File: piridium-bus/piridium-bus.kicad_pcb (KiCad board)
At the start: 2 copper layers, 52 parts, among them J1 EPS, J2 MODEM UART, J3 ANT, J4 PAYLOAD, Q1 2N7002, Q2 DMP3015LSSQ, U1 LM1117-3.3, U2 TPS54394RSAR, U3 MAX6369, U4 74LS126, U5 DS3232M

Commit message: some work on routing
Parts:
- removed H1, H2, H3, H4: M3, MountingHole:MountingHole_3.2mm_M3_DIN965_Pad
- added MH1: M3, MountingHole:MountingHole_3.2mm_M3_DIN965_Pad, F.Cu at (110.5, 55.9)
- added MH2: M3, MountingHole:MountingHole_3.2mm_M3_DIN965_Pad, F.Cu at (184.2, 55.9)
- added MH3: M3, MountingHole:MountingHole_3.2mm_M3_DIN965_Pad, F.Cu at (186.7, 141.6)
- added MH4: M3, MountingHole:MountingHole_3.2mm_M3_DIN965_Pad, F.Cu at (106.7, 141.6)
- BT1: moved to B.Cu
- C6, C7: footprint Capacitor_SMD:C_0805_2012Metric -> Capacitor_SMD:C_0603_1608Metric
- moved U2 176.1 mm to (253.5, 92.5)
- moved L2 161.9 mm to (253.0, 81.3), turned to 90 degrees
- moved C1 156.5 mm to (285.6, 103.6)
- moved C6 154.7 mm to (249.4, 94.5), turned to -90 degrees
- moved C13 150.7 mm to (316.0, 78.4)
- moved C8 148.7 mm to (301.4, 91.2)
- moved R8 147.3 mm to (311.4, 84.6)
- moved R7 143.8 mm to (301.4, 94.2)
- moved U1 140.6 mm to (287.0, 134.1)
- moved C12 137.7 mm to (252.5, 131.1)
- moved C14 137.6 mm to (276.3, 112.3)
- moved C4 137.1 mm to (251.5, 97.5)
- moved L1 136.2 mm to (253.0, 103.6), turned to 90 degrees
- moved JP1 134.1 mm to (268.7, 132.3)
- moved R3 131.7 mm to (331.7, 65.4)
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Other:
- board outline added: 90.2 x 95.9 mm

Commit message: routing work on bus
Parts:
- added R12: 10K, Resistor_SMD:R_1206_3216Metric, F.Cu at (111.3, 75.2)
- C1, C10, C11, C2, C3, C4, C5, C6, C7, C8, C9, JP1, L1, L2, R1, R2, R5, R6, TP1, TP2, TP3, TP4, U1, U2, U3: moved to B.Cu
- R10, R7, R8: footprint Resistor_SMD:R_0805_2012Metric -> Resistor_SMD:R_1206_3216Metric
- R11: value 10K -> 33K; footprint Resistor_SMD:R_0805_2012Metric -> Resistor_SMD:R_1206_3216Metric
- R3, R4: footprint Resistor_SMD:R_0805_2012Metric -> Resistor_SMD:R_1206_3216Metric; moved to B.Cu
- R9: value 10K -> 22K; footprint Resistor_SMD:R_0805_2012Metric -> Resistor_SMD:R_1206_3216Metric
- moved R3 205.9 mm to (131.0, 111.4), turned to 180 degrees
- moved D1 188.1 mm to (113.8, 75.2), turned to 90 degrees
- moved R6 183.1 mm to (124.4, 115.8)
- moved C8 178.5 mm to (124.4, 113.8)
- moved R9 169.1 mm to (138.2, 75.2)
- moved R8 157.6 mm to (155.4, 62.0), turned to -90 degrees
- moved R1 157.0 mm to (123.8, 107.7), turned to -90 degrees
- moved TP3 152.9 mm to (115.3, 132.6), turned to 90 degrees
- moved R5 152.4 mm to (123.8, 118.9), turned to 90 degrees
- moved U1 151.8 mm to (137.1, 110.3), turned to 90 degrees
- moved C10 149.4 mm to (119.3, 134.6)
- moved C1 149.0 mm to (137.1, 115.9)
- moved R7 146.5 mm to (159.0, 59.4)
- moved C11 146.5 mm to (119.3, 131.1)
- moved TP4 143.6 mm to (125.5, 132.6), turned to -90 degrees
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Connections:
- R11 pad 1: /SUP_OUT -> GND
- R11 pad 2: Net-(D1-Pad2) -> S_MODEM_ON_OFF
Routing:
- net GND: track 0.01 -> 46.1 mm, vias 0 -> 14
- net +5VP: track 0.00 -> 35.9 mm, vias 0 -> 2
- net Net-(BT1-Pad1): track 0.00 -> 35.3 mm
- net +5V: track 0.00 -> 32.5 mm, vias 0 -> 2
- net +BATT: track 0.00 -> 24.5 mm
- net Net-(C5-Pad1): track 0.00 -> 23.0 mm
- net Net-(C7-Pad2): track 0.00 -> 10.7 mm, vias 0 -> 4
- net Net-(C6-Pad2): track 0.00 -> 10.7 mm, vias 0 -> 4
- net /EN: track 0.00 -> 8.17 mm
- net Net-(R5-Pad2): track 0.00 -> 5.16 mm
- net Net-(R1-Pad2): track 0.00 -> 5.16 mm
- net Net-(JP1-Pad1): track 0.00 -> 3.76 mm
- net +3.3V: track 0.00 -> 2.90 mm
- net S_HANDSHAKE: track 0.00 -> 2.83 mm
- net /PAYLOAD_PWR: track 0.00 -> 2.54 mm
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- added copper zone on B.Cu, net GND
- added copper zone on B.Cu, net Net-(C6-Pad2)
- added copper zone on B.Cu, net Net-(C7-Pad2)
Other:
- outline, holes or cut-outs redrawn

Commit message: update routing
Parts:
- J1: footprint Connector_Molex:Molex_Nano-Fit_105313-xx04_1x04_P2.50mm_Horizontal -> Connector_PinHeader_2.54mm:PinHeader_1x04_P2.54mm_Horizontal; moved to B.Cu
- J4: footprint Connector_Molex:Molex_Nano-Fit_105314-xx10_2x05_P2.50mm_Horizontal -> Connector_PinHeader_2.54mm:PinHeader_2x05_P2.54mm_Vertical
- JP1: moved to F.Cu
- R11, R9: moved to B.Cu
- moved J2 95.6 mm to (165.9, 141.2), turned to -90 degrees
- moved J3 85.1 mm to (144.0, 140.0), turned to 180 degrees
- moved A2 71.5 mm to (166.4, 62.5), turned to 0 degrees
- moved C12 49.8 mm to (158.0, 103.9), turned to -90 degrees
- moved R12 45.3 mm to (150.4, 98.0)
- moved D1 45.3 mm to (152.9, 98.0)
- moved U4 43.1 mm to (153.1, 107.1), turned to 0 degrees
- moved A3 42.2 mm to (148.0, 88.8), turned to -90 degrees
- moved R11 34.2 mm to (135.1, 108.5), turned to -90 degrees
- moved R9 33.3 mm to (137.7, 108.5), turned to -90 degrees
- moved J4 30.3 mm to (135.9, 65.8)
- moved R7 24.0 mm to (147.6, 80.6), turned to -90 degrees
- moved Q1 23.2 mm to (144.5, 80.6), turned to -90 degrees
- moved BT1 23.1 mm to (177.5, 117.6)
- moved C13 23.1 mm to (182.6, 119.1)
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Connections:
- A3 pad 22: GND -> GNDS
- J3 pad 2: GND -> GNDS
- J4 pad 2: SPI_MOSI -> I2C_SCL
- J4 pad 3: SPI_MISO -> SPI_MOSI
- J4 pad 4: SPI_SCK -> I2C_SDA
- J4 pad 5: GND -> SPI_MISO
- J4 pad 6: I2C_SCL -> SPI_CE0
- J4 pad 7: I2C_SDA -> SPI_SCK
- J4 pad 8: SPI_CE0 -> SPI_CE1
- J4 pad 9: SPI_CE1 -> GND
- R9 pad 1: +5V -> +5VP
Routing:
- net I2C_SDA: track 0.00 -> 77.4 mm
- net I2C_SCL: track 0.00 -> 68.3 mm
- net UART_RX: track 0.00 -> 28.7 mm, vias 0 -> 2
- net UART_TX: track 0.00 -> 27.9 mm, vias 0 -> 2
- net +3.3V: track 2.90 -> 30.2 mm
- net Net-(A3-Pad21): track 0.00 -> 19.5 mm
- net /SUP_OUT: track 0.00 -> 14.9 mm
- net Net-(A3-Pad13): track 0.00 -> 13.5 mm, vias 0 -> 2
- net +5VP: track 35.9 -> 46.2 mm, vias 2 -> 3
- net unconnected-(A3-Pad24): track 0.00 -> 10.2 mm
- net Net-(A3-Pad6): track 0.00 -> 7.54 mm
- net S_MODEM_ON_OFF: track 0.00 -> 7.34 mm, vias 0 -> 1
- net Net-(Q1-Pad3): track 0.00 -> 5.83 mm
- net GND: track 46.1 -> 51.1 mm
- net Net-(Q1-Pad1): track 0.00 -> 4.86 mm
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- added copper zone on F.Cu, net GNDS
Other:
- outline, holes or cut-outs redrawn

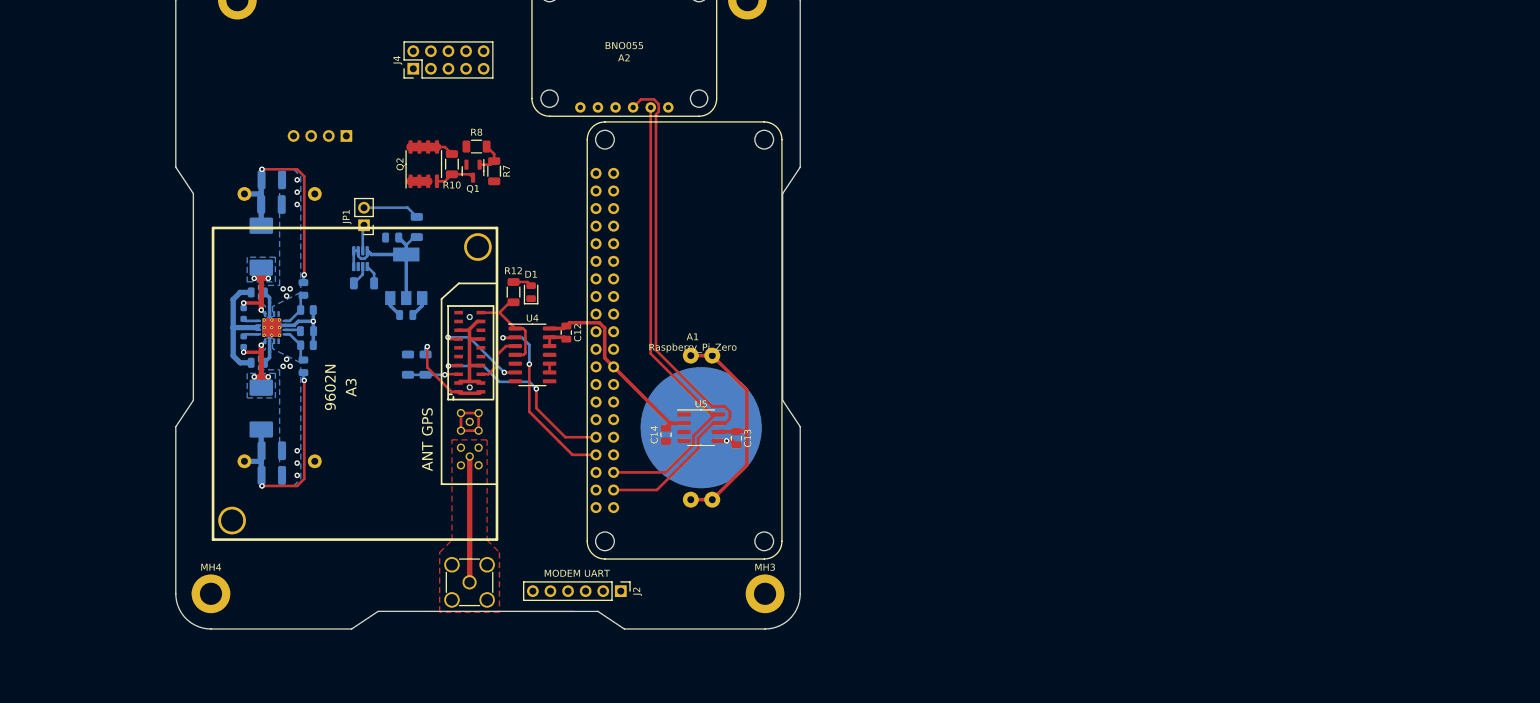
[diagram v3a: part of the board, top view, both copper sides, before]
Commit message: add inhibits, telemetry, and solar to bus
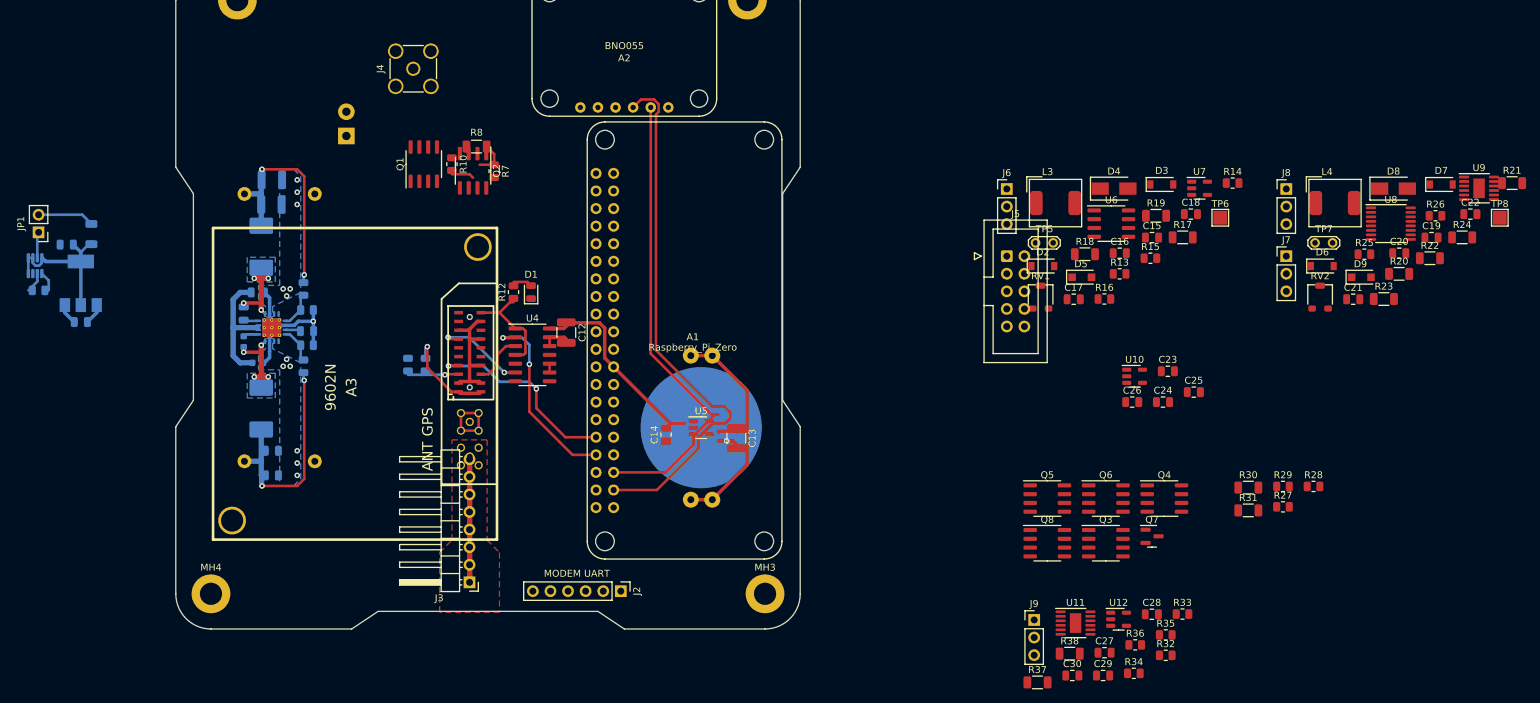
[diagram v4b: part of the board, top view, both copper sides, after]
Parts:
- added C15: 0.1uF, Capacitor_SMD:C_0805_2012Metric, F.Cu at (242.6, 90.2)
- added C16: 1uF, Capacitor_SMD:C_0805_2012Metric, F.Cu at (237.9, 92.4)
- added C17: 1uF, Capacitor_SMD:C_0805_2012Metric, F.Cu at (231.3, 99.1)
- added C18: 0.1uF, Capacitor_SMD:C_0805_2012Metric, F.Cu at (248.2, 86.8)
- added C19: 0.1uF, Capacitor_SMD:C_0805_2012Metric, F.Cu at (282.9, 90.2)
- added C20: 10uF, Capacitor_SMD:C_0805_2012Metric, F.Cu at (278.3, 92.4)
- added C21: 0.1uF, Capacitor_SMD:C_0805_2012Metric, F.Cu at (271.6, 99.1)
- added C22: 10uF, Capacitor_SMD:C_0805_2012Metric, F.Cu at (288.5, 86.8)
- added C23: 1uF, Capacitor_SMD:C_0805_2012Metric, F.Cu at (244.9, 109.5)
- added C24: 10uF, Capacitor_SMD:C_0805_2012Metric, F.Cu at (244.2, 113.9)
- added C25: 0.1uF, Capacitor_SMD:C_0805_2012Metric, F.Cu at (248.6, 112.5)
- added C26: 0.1uF, Capacitor_SMD:C_0805_2012Metric, F.Cu at (239.7, 113.9)
- added C27: 10uF, Capacitor_SMD:C_0805_2012Metric, F.Cu at (235.7, 150.1)
- added C28: 1uF, Capacitor_SMD:C_0805_2012Metric, F.Cu at (242.5, 144.6)
- added C29: 10uF, Capacitor_SMD:C_0805_2012Metric, F.Cu at (235.5, 153.4)
- added C30: 0.1uF, Capacitor_SMD:C_0805_2012Metric, F.Cu at (231.1, 153.4)
- added D2: DFLS130L-7, Diode_SMD:D_SOD-123, F.Cu at (226.8, 94.3)
- added D3: DFLS130L-7, Diode_SMD:D_SOD-123, F.Cu at (244.0, 82.5)
- added D4: CMSH3-40MA, Diode_SMD:D_SMA, F.Cu at (237.1, 83.1)
- added D5: RB051MM-2Y, Diode_SMD:D_SOD-123F, F.Cu at (232.4, 95.9)
- added D6: DFLS130L-7, Diode_SMD:D_SOD-123, F.Cu at (267.2, 94.3)
- added D7: DFLS130L-7, Diode_SMD:D_SOD-123, F.Cu at (284.3, 82.5)
- added D8: CMSH3-40MA, Diode_SMD:D_SMA, F.Cu at (277.4, 83.1)
- added D9: RB051MM-2Y, Diode_SMD:D_SOD-123F, F.Cu at (272.8, 95.9)
- added J5: PAYLOAD, Connector_IDC:IDC-Header_2x05_P2.54mm_Vertical, F.Cu at (221.6, 92.8)
- added J6: IN1, Connector_PinHeader_2.54mm:PinHeader_1x03_P2.54mm_Vertical, F.Cu at (221.6, 83.2)
- added J7: IN2, Connector_PinHeader_2.54mm:PinHeader_1x03_P2.54mm_Vertical, F.Cu at (262.0, 92.8)
- added J8: IN1, Connector_PinHeader_2.54mm:PinHeader_1x03_P2.54mm_Vertical, F.Cu at (262.0, 83.2)
- added J9: IN2, Connector_PinHeader_2.54mm:PinHeader_1x03_P2.54mm_Vertical, F.Cu at (225.6, 145.4)
- added L3: 10uH, Inductor_SMD:L_AVX_LMLP07A7, F.Cu at (228.6, 85.2)
- added L4: 10uH, Inductor_SMD:L_AVX_LMLP07A7, F.Cu at (269.0, 85.2)
- added Q3: DMP3015LSSQ, Package_SO:SOIC-8_3.9x4.9mm_P1.27mm, F.Cu at (235.9, 134.3)
- added Q4: Si4186DY, Package_SO:SOIC-8_3.9x4.9mm_P1.27mm, F.Cu at (244.4, 127.9)
- added Q5: DMP3015LSSQ, Package_SO:SOIC-8_3.9x4.9mm_P1.27mm, F.Cu at (227.5, 127.9)
- added Q6: DMP3015LSSQ, Package_SO:SOIC-8_3.9x4.9mm_P1.27mm, F.Cu at (235.9, 127.9)
- added Q7: 2N7002, Package_TO_SOT_SMD:SOT-23, F.Cu at (242.6, 133.3)
- added Q8: DMP3015LSSQ, Package_SO:SOIC-8_3.9x4.9mm_P1.27mm, F.Cu at (227.5, 134.3)
- added R13: 100R, Resistor_SMD:R_0805_2012Metric, F.Cu at (237.9, 95.4)
- added R14: 100K, Resistor_SMD:R_0805_2012Metric, F.Cu at (254.2, 82.3)
- added R15: 200K, Resistor_SMD:R_0805_2012Metric, F.Cu at (242.3, 93.2)
- added R16: 100K, Resistor_SMD:R_0805_2012Metric, F.Cu at (235.7, 99.0)
- added R17: 4m, Resistor_SMD:R_1206_3216Metric, F.Cu at (247.0, 90.1)
- added R18: 100R, Resistor_SMD:R_1206_3216Metric, F.Cu at (232.9, 92.6)
- added R19: 10K, Resistor_SMD:R_1206_3216Metric, F.Cu at (243.2, 87.0)
- added R20: 22K, Resistor_SMD:R_1206_3216Metric, F.Cu at (278.2, 95.4)
- added R21: 10K, Resistor_SMD:R_1206_3216Metric, F.Cu at (294.6, 82.3)
- added R22: 33K, Resistor_SMD:R_1206_3216Metric, F.Cu at (282.7, 93.2)
- added R23: 10K, Resistor_SMD:R_1206_3216Metric, F.Cu at (276.1, 99.0)
- added R24: 4m, Resistor_SMD:R_1206_3216Metric, F.Cu at (287.4, 90.1)
- added R25: 75K, Resistor_SMD:R_0805_2012Metric, F.Cu at (273.2, 92.6)
- added R26: 10K, Resistor_SMD:R_0805_2012Metric, F.Cu at (283.5, 87.0)
- added R27: 191K, Resistor_SMD:R_0805_2012Metric, F.Cu at (261.5, 129.1)
- added R28: 147K, Resistor_SMD:R_0805_2012Metric, F.Cu at (265.9, 126.1)
- added R29: 97.6K, Resistor_SMD:R_0805_2012Metric, F.Cu at (261.5, 126.1)
- added R30: 50m, Resistor_SMD:R_1206_3216Metric, F.Cu at (256.5, 126.3)
- added R31: 4m, Resistor_SMD:R_1206_3216Metric, F.Cu at (256.5, 129.6)
- added R32: 75K, Resistor_SMD:R_0805_2012Metric, F.Cu at (244.6, 150.5)
- added R33: 10K, Resistor_SMD:R_0805_2012Metric, F.Cu at (247.0, 144.5)
- added R34: 191K, Resistor_SMD:R_0805_2012Metric, F.Cu at (239.9, 153.1)
- added R35: 147K, Resistor_SMD:R_0805_2012Metric, F.Cu at (244.6, 147.5)
- added R36: 97.6K, Resistor_SMD:R_0805_2012Metric, F.Cu at (240.1, 149.0)
- added R37: 50m, Resistor_SMD:R_1206_3216Metric, F.Cu at (226.0, 154.4)
- added R38: 4m, Resistor_SMD:R_1206_3216Metric, F.Cu at (230.7, 150.3)
- added RV1: 100K, piridium-bus:Bourns PVG3A, F.Cu at (226.5, 98.8)
- added RV2: 100K, piridium-bus:Bourns PVG3A, F.Cu at (266.8, 98.8)
- added TP5: VIN, TestPoint:TestPoint_2Pads_Pitch2.54mm_Drill0.8mm, F.Cu at (225.8, 90.9)
- added TP6: Vmpp, TestPoint:TestPoint_Pad_2.0x2.0mm, F.Cu at (252.4, 87.3)
- added TP7: VIN, TestPoint:TestPoint_2Pads_Pitch2.54mm_Drill0.8mm, F.Cu at (266.1, 90.9)
- added TP8: Vmpp, TestPoint:TestPoint_Pad_2.0x2.0mm, F.Cu at (292.8, 87.3)
- added U10: INA180A3, Package_TO_SOT_SMD:SOT-23-5, F.Cu at (240.1, 110.2)
- added U11: LT3652EMSE, Package_SO:MSOP-12-1EP_3x4mm_P0.65mm_EP1.65x2.85mm, F.Cu at (231.5, 145.8)
- added U12: INA180A3, Package_TO_SOT_SMD:SOT-23-5, F.Cu at (237.7, 145.3)
- added U6: DS3232M, Package_SO:SOIC-8_3.9x4.9mm_P1.27mm, F.Cu at (236.7, 88.2)
- added U7: INA180A3, Package_TO_SOT_SMD:SOT-23-5, F.Cu at (249.4, 83.0)
- added U8: ADS7828, Package_SO:TSSOP-16_4.4x5mm_P0.65mm, F.Cu at (277.1, 88.2)
- added U9: LT3652EMSE, Package_SO:MSOP-12-1EP_3x4mm_P0.65mm_EP1.65x2.85mm, F.Cu at (289.8, 83.0)
- C10: value 22uF -> 1uF; footprint Capacitor_SMD:C_1210_3225Metric -> Capacitor_SMD:C_0805_2012Metric
- C11: value 22uF -> 10uF; footprint Capacitor_SMD:C_1210_3225Metric -> Capacitor_SMD:C_0805_2012Metric
- C12: value 0.1uF -> 22uF; footprint Capacitor_SMD:C_0805_2012Metric -> Capacitor_SMD:C_1210_3225Metric
- C13: value 1uF -> 22uF; footprint Capacitor_SMD:C_0805_2012Metric -> Capacitor_SMD:C_1210_3225Metric
- C14, C8: value 1uF -> 0.1uF
- C6: footprint Capacitor_SMD:C_0603_1608Metric -> Capacitor_SMD:C_0805_2012Metric
- C9: value 10uF -> 0.1uF; footprint Capacitor_SMD:C_0805_2012Metric -> Capacitor_SMD:C_0603_1608Metric
- J1: footprint Connector_PinHeader_2.54mm:PinHeader_1x04_P2.54mm_Horizontal -> TerminalBlock_Phoenix:TerminalBlock_Phoenix_PT-1,5-2-3.5-H_1x02_P3.50mm_Horizontal
- J3: value ANT -> INHIBITS; footprint Connector_Coaxial:SMA_Amphenol_901-144_Vertical -> Connector_PinHeader_2.54mm:PinHeader_1x08_P2.54mm_Horizontal
- J4: value PAYLOAD -> ANT; footprint Connector_PinHeader_2.54mm:PinHeader_2x05_P2.54mm_Vertical -> Connector_Coaxial:SMA_Amphenol_901-144_Vertical
- Q1: value 2N7002 -> DMP3015LSSQ; footprint Package_TO_SOT_SMD:SOT-23 -> Package_SO:SOIC-8_3.9x4.9mm_P1.27mm
- Q2: value DMP3015LSSQ -> Si4186DY
- R10: value 10K -> 124K; footprint Resistor_SMD:R_1206_3216Metric -> Resistor_SMD:R_0805_2012Metric
- R11: value 33K -> 22.1K; footprint Resistor_SMD:R_1206_3216Metric -> Resistor_SMD:R_0805_2012Metric
- R12: value 10K -> 100K; footprint Resistor_SMD:R_1206_3216Metric -> Resistor_SMD:R_0805_2012Metric
- R3: footprint Resistor_SMD:R_1206_3216Metric -> Resistor_SMD:R_0805_2012Metric
- R5: value 124K -> 100R
- R6: value 22.1K -> 100R
- R7: value 100R -> 100K; footprint Resistor_SMD:R_1206_3216Metric -> Resistor_SMD:R_0805_2012Metric
- R8: value 10K -> 100K
- R9: value 22K -> 100R; footprint Resistor_SMD:R_1206_3216Metric -> Resistor_SMD:R_0805_2012Metric
- U5: value DS3232M -> INA180A3; footprint Package_SO:SOIC-8_3.9x4.9mm_P1.27mm -> Package_TO_SOT_SMD:SOT-23-5
- moved C5 47.0 mm to (85.9, 91.2)
- moved U3 47.0 mm to (81.3, 94.2)
- moved C1 47.0 mm to (87.9, 102.4)
- moved JP1 47.0 mm to (81.8, 89.4)
- moved R3 47.0 mm to (81.8, 97.8)
- moved R4 47.0 mm to (89.4, 89.7)
- moved U1 47.0 mm to (87.9, 96.8)
- moved Q1 7.18 mm to (137.4, 79.6), turned to 90 degrees
- moved Q2 7.18 mm to (144.5, 80.5), turned to -90 degrees
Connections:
- C10 pad 1: +5VP -> Net-(C10-Pad1)
- C11 pad 1: +5VP -> +BATT
- C12 pad 1: +3.3V -> +5VP
- C13 pad 1: Net-(BT1-Pad1) -> +5VP
- C14 pad 1: GND -> +3.3V
- C14 pad 2: +3.3V -> GND
- C6 pad 2: Net-(C6-Pad2) -> /A1L
- C8 pad 1: Net-(C8-Pad1) -> /A2H
- C8 pad 2: GND -> Net-(C8-Pad2)
- C9 pad 1: +BATT -> Net-(C9-Pad1)
- C9 pad 2: GND -> Net-(C9-Pad2)
- J1 pad 1: +BATT -> Net-(Q1-Pad5)
- J1 pad 2: I2C_SCL -> Net-(Q2-Pad5)
- J3 pad 1: Net-(A3-Pad21) -> /B1H
- J3 pad 2: GNDS -> /B1L
- J4 pad 1: /PAYLOAD_PWR -> Net-(A3-Pad21)
- J4 pad 2: I2C_SCL -> GNDS
- L1 pad 2: Net-(C6-Pad2) -> Net-(C7-Pad2)
- L2 pad 1: Net-(C7-Pad2) -> Net-(C9-Pad2)
- Q1 pad 1: Net-(Q1-Pad1) -> Net-(C6-Pad1)
- Q1 pad 2: GND -> Net-(C6-Pad1)
- Q1 pad 3: Net-(Q1-Pad3) -> Net-(C6-Pad1)
- Q2 pad 1: /PAYLOAD_PWR -> Net-(C8-Pad2)
- Q2 pad 2: /PAYLOAD_PWR -> Net-(C8-Pad2)
- Q2 pad 3: /PAYLOAD_PWR -> Net-(C8-Pad2)
- Q2 pad 4: Net-(Q1-Pad3) -> /A2H
- Q2 pad 5: +BATT -> Net-(Q2-Pad5)
- Q2 pad 6: +BATT -> Net-(Q2-Pad5)
- Q2 pad 7: +BATT -> Net-(Q2-Pad5)
- Q2 pad 8: +BATT -> Net-(Q2-Pad5)
- R10 pad 1: +BATT -> +5VP
- R10 pad 2: Net-(Q1-Pad3) -> Net-(R10-Pad2)
- R11 pad 1: GND -> Net-(R10-Pad2)
- R11 pad 2: S_MODEM_ON_OFF -> GND
- R12 pad 1: /SUP_OUT -> /B1L
- R12 pad 2: Net-(D1-Pad2) -> GND
- R3 pad 1: S_HANDSHAKE -> /A1L
- R3 pad 2: GND -> Net-(C8-Pad2)
- R4 pad 1: Net-(C5-Pad1) -> S_HANDSHAKE
- R4 pad 2: /EN -> GND
- R5 pad 1: +5VP -> /A2L
- R5 pad 2: Net-(R5-Pad2) -> Net-(C8-Pad2)
- R6 pad 1: Net-(R5-Pad2) -> Net-(C6-Pad1)
- R6 pad 2: GND -> /A1H
- R7 pad 1: Net-(Q1-Pad1) -> Net-(C6-Pad1)
- R7 pad 2: S_PAYLOAD_PWR -> /A2H
- R8 pad 1: Net-(Q1-Pad1) -> Net-(C5-Pad1)
- R8 pad 2: GND -> /EN
- R9 pad 1: +5VP -> /CHARGE_OUT
- R9 pad 2: S_MODEM_ON_OFF -> /B1H
- U2 pad 1: Net-(C7-Pad1) -> Net-(C9-Pad1)
- U2 pad 11: Net-(C8-Pad1) -> Net-(C10-Pad1)
- U2 pad 12: Net-(R5-Pad2) -> Net-(R10-Pad2)
- U2 pad 16: Net-(C7-Pad2) -> Net-(C9-Pad2)
- U2 pad 4: Net-(C6-Pad1) -> Net-(C7-Pad1)
- U2 pad 5: Net-(C6-Pad2) -> Net-(C7-Pad2)
- U5 pad 1: unconnected-(U5-Pad1) -> TELEM_IBAT
- U5 pad 2: +3.3V -> GND
- U5 pad 3: unconnected-(U5-Pad3) -> Net-(Q6-Pad5)
- U5 pad 4: unconnected-(U5-Pad4) -> +BATT
- U5 pad 5: GND -> +3.3V
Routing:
- net I2C_SCL: track 68.3 -> 145.7 mm
- net I2C_SDA: track 77.4 -> 0.00 mm
- net /B1H: track 0.00 -> 26.8 mm, vias 0 -> 1
- net Net-(A3-Pad21): track 19.5 -> 0.00 mm
- net Net-(C9-Pad2): track 0.00 -> 10.7 mm, vias 0 -> 4
- net Net-(C6-Pad2): track 10.7 -> 0.00 mm, vias 4 -> 0
- net Net-(C8-Pad2): track 0.00 -> 8.10 mm
- net S_MODEM_ON_OFF: track 7.34 -> 0.00 mm, vias 1 -> 0
- net +BATT: track 27.1 -> 20.7 mm
- net Net-(Q1-Pad3): track 5.83 -> 0.00 mm
- net Net-(R5-Pad2): track 5.16 -> 0.00 mm
- net Net-(Q1-Pad1): track 4.86 -> 0.00 mm
- net Net-(C6-Pad1): track 2.22 -> 7.07 mm
- net Net-(R10-Pad2): track 0.00 -> 3.25 mm
- net GND: track 51.1 -> 48.1 mm, vias 14 -> 13
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- removed copper zone on B.Cu, net Net-(C6-Pad2)

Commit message: fix bus board messup, remove redundant components from eps
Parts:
- added C19: 0.1uF, Capacitor_SMD:C_0805_2012Metric, F.Cu at (297.2, 127.0)
- added C20: 10uF, Capacitor_SMD:C_0805_2012Metric, F.Cu at (297.2, 130.0)
- added U8: MCP3208, Package_SO:SOIC-16_3.9x9.9mm_P1.27mm, F.Cu at (290.7, 131.2)
- C12, C13, R10, R20, R22, R8: moved to B.Cu
- C6, C8, J1, R3, R5, R6, R9: moved to F.Cu
- U4: value 74LS126 -> 74HC126
- moved R22 148.4 mm to (135.1, 108.5), turned to -90 degrees
- moved R20 141.2 mm to (137.7, 108.5), turned to -90 degrees
- moved R23 125.7 mm to (150.4, 98.0), turned to 90 degrees
- moved J5 90.3 mm to (137.2, 61.0), turned to 90 degrees
- moved R9 85.0 mm to (208.0, 156.2)
- moved J4 74.6 mm to (144.0, 140.0)
- moved J3 73.6 mm to (70.4, 141.0)
- moved R12 73.5 mm to (184.2, 163.3)
- moved Q2 71.4 mm to (83.1, 116.8)
- moved C13 67.4 mm to (115.4, 124.2), turned to 0 degrees
- moved U6 66.1 mm to (177.5, 117.6)
- moved C17 62.2 mm to (172.2, 118.6), turned to 90 degrees
- moved C16 61.4 mm to (182.6, 119.1), turned to -90 degrees
- moved R8 57.0 mm to (89.4, 89.7), turned to 90 degrees
- moved R7 51.9 mm to (97.0, 92.2)
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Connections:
- A1 pad 35: unconnected-(A1-Pad35) -> ADC_CS
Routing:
- net I2C_SCL: track 145.7 -> 67.3 mm
- net I2C_SDA: track 0.00 -> 77.4 mm
- net /B1H: track 26.8 -> 0.00 mm, vias 1 -> 0
- net Net-(A3-Pad21): track 0.00 -> 19.5 mm
- net Net-(C8-Pad2): track 8.10 -> 0.00 mm
- net S_MODEM_ON_OFF: track 0.00 -> 7.37 mm, vias 0 -> 1
- net Net-(C6-Pad1): track 7.07 -> 0.00 mm
- net GND: track 48.1 -> 51.0 mm, vias 13 -> 14
- net Net-(BT1-Pad1): track 38.2 -> 35.3 mm, vias 1 -> 0
- net Net-(D1-Pad2): track 0.00 -> 2.76 mm
- net Net-(C9-Pad1): track 0.00 -> 2.35 mm
- net Net-(C10-Pad1): track 0.00 -> 2.24 mm
- net /A2H: track 2.24 -> 0.00 mm
- net Net-(R10-Pad2): track 3.25 -> 5.15 mm
- added copper zone on B.Cu, net Net-(C9-Pad2)

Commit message: ngl not sure what I did here
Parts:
- removed the C19 at (282.9, 90.2)
- removed the C20 at (278.3, 92.4)
- removed the U8 at (277.1, 88.2)
- R18, R19, R21, R4, R8: footprint Resistor_SMD:R_1206_3216Metric -> Resistor_SMD:R_0805_2012Metric
- moved R24 151.8 mm to (137.2, 68.1), turned to -90 degrees
- moved R21 150.4 mm to (144.5, 72.6), turned to 90 degrees
- moved Q7 119.9 mm to (141.5, 68.8), turned to -90 degrees
- moved C18 118.3 mm to (131.3, 68.3), turned to -90 degrees
- moved U7 116.3 mm to (134.1, 68.1), turned to 90 degrees
- moved Q8 106.7 mm to (139.7, 73.7), turned to 180 degrees
- moved R19 103.9 mm to (141.5, 65.8), turned to 180 degrees
- moved R18 90.5 mm to (145.5, 68.8), turned to -90 degrees
- moved C13 14.8 mm to (127.3, 115.5)
- moved C3 14.8 mm to (127.3, 73.4)
- moved C9 14.8 mm to (123.2, 96.5)
- moved L2 14.8 mm to (125.9, 106.2)
- moved R11 14.8 mm to (132.5, 97.0)
- moved R2 14.8 mm to (132.5, 91.9)
- moved TP1 14.8 mm to (123.4, 75.2)
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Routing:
- net Net-(Q8-Pad5): track 0.00 -> 8.29 mm
- net /PAYLOAD_PWR: track 0.00 -> 7.88 mm
- net Net-(Q7-Pad1): track 0.00 -> 5.25 mm
- net Net-(Q7-Pad3): track 0.00 -> 4.63 mm
- net +BATT: track 20.7 -> 23.3 mm
- net GND: track 51.0 -> 50.3 mm

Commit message: routing work
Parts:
- moved R14 201.6 mm to (52.8, 92.2), turned to 180 degrees
- moved R13 185.1 mm to (52.8, 90.2), turned to 180 degrees
- moved Q6 179.7 mm to (60.6, 88.0)
- moved Q4 175.3 mm to (82.5, 60.5), turned to 90 degrees
- moved Q5 172.3 mm to (62.0, 80.0)
- moved Q3 166.5 mm to (81.3, 72.6), turned to 90 degrees
- moved R9 158.4 mm to (61.2, 96.8)
- moved R12 152.4 mm to (55.6, 81.4)
- moved C19 151.3 mm to (154.0, 78.1), turned to -90 degrees
- moved U8 150.2 mm to (149.1, 81.3)
- moved C20 149.7 mm to (156.8, 78.1), turned to -90 degrees
- moved J3 82.9 mm to (108.4, 67.3), turned to 0 degrees
- moved R6 57.0 mm to (64.5, 64.5)
- moved Q2 56.7 mm to (77.0, 60.5), turned to 90 degrees
- moved R5 52.0 mm to (70.4, 66.3)
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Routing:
- net +5VP: track 46.1 -> 71.7 mm, vias 3 -> 4
- net Net-(C6-Pad1): track 0.00 -> 12.9 mm
- net Net-(C8-Pad2): track 0.00 -> 12.7 mm
- net /A1L: track 0.00 -> 10.6 mm
- net /A2H: track 0.00 -> 10.6 mm
- net +3.3V: track 30.3 -> 20.0 mm, vias 0 -> 1
- net +BATT: track 23.3 -> 25.8 mm
- net +5V: track 32.5 -> 35.0 mm
- net GND: vias 14 -> 15
- added copper zone on In1.Cu, net +3.3V
- added copper zone on In2.Cu, net GND
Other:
- copper layers 2 -> 4
